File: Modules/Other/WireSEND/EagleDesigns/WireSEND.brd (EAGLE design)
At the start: 100 x 80 mm, 2 parts

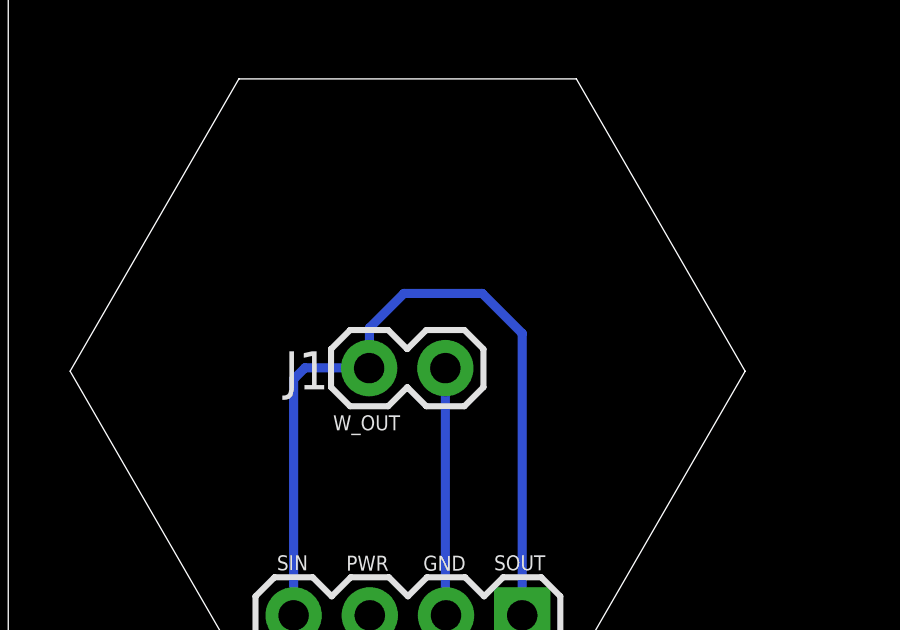
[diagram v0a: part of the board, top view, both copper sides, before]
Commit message: added version numbers, and deleted most of the text that was on each module.
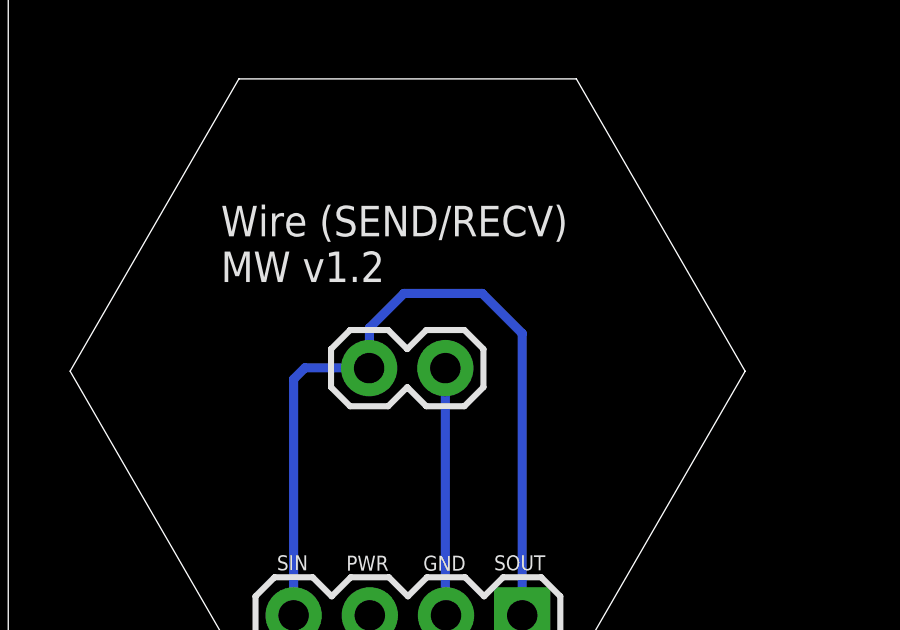
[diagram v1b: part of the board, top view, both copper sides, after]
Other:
- board text added: "Wire (SEND/RECV) MW v1.2"
- board text removed: "W_OUT"
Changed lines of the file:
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@@
 <layer number="24" name="bOrigins" color="15" fill="1" visible="yes" active="yes"/>
 <layer number="25" name="tNames" color="7" fill="1" visible="yes" active="yes"/>
-<layer number="26" name="bNames" color="7" fill="1" visible="no" active="yes"/>
+<layer number="26" name="bNames" color="7" fill="1" visible="yes" active="yes"/>
 <layer number="27" name="tValues" color="7" fill="1" visible="yes" active="yes"/>
 <layer number="28" name="bValues" color="7" fill="1" visible="yes" active="yes"/>
@@
 <text x="13.8323" y="5.388" size="0.5" layer="21">GND</text>
 <text x="16.1945" y="5.4007" size="0.5" layer="21">SOUT</text>
-<text x="10.8269" y="10.068" size="0.5" layer="21">W_OUT</text>
+<text x="7.09" y="15.01" size="1.016" layer="21">Wire (SEND/RECV)
+MW v1.2</text>
 </plain>
 <attributes>
@@
 </element>
 <element name="J1" library="SparkFun-Connectors" package="1X02" value="" x="14.57" y="12.14" smashed="yes" rot="R180">
-<attribute name="NAME" x="10.6762" y="12.7012" size="1.27" layer="25" ratio="10" rot="R180"/>
 <attribute name="VALUE" x="15.84" y="15.315" size="1.27" layer="27" rot="R180"/>
 </element>
@@
 </board>
 </drawing>
+<compatibility>
+<note version="6.3" minversion="6.2.2" severity="warning">
+Since Version 6.2.2 text objects can contain more than one line,
+which will not be processed correctly with this version.
+</note>
+</compatibility>
 </eagle>
